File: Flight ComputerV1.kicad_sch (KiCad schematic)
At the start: 28 parts, among them J101 ICSP, J102 Screw_Terminal_01x02, J103 Conn_01x08, J104 Conn_01x07, J105 Micro_SD_Card, J106 Conn_02x10_Top_Bottom, SW101 1-1825910-8, U101 ATmega328PB-A, U102 LMT84DCK

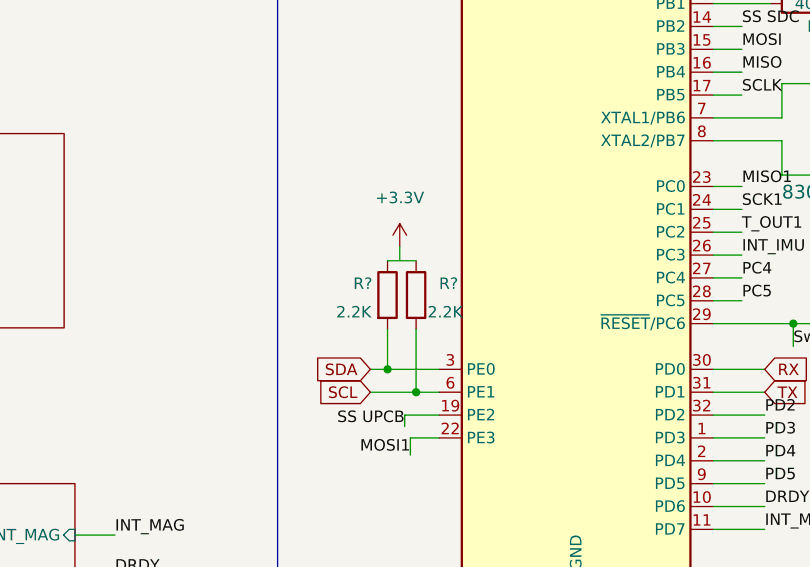
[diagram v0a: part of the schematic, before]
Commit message: Updated all trace widths and pull-up res.
I'm having a problem when I try to update the pcb with the pull-up resistors. Can you guys try updating the pcb, and let me know if you run into any errors?
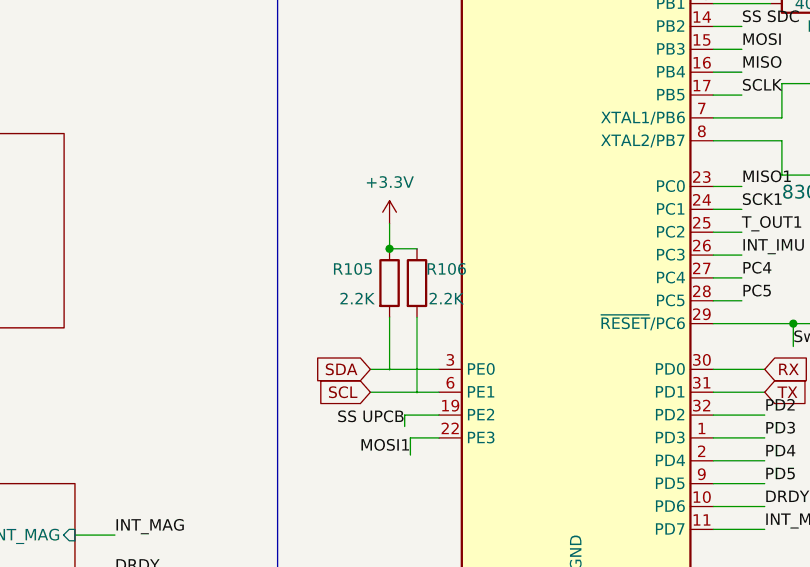
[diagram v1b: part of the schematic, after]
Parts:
- removed R? (x2): 2.2K, Resistor_SMD:R_0603_1608Metric_Pad0.98x0.95mm_HandSolder, symbol Device:R
- added R105, R106: 2.2K, Resistor_SMD:R_0603_1608Metric_Pad0.98x0.95mm_HandSolder, symbol Device:R
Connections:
- net +3V3: now also R105.1, R106.1

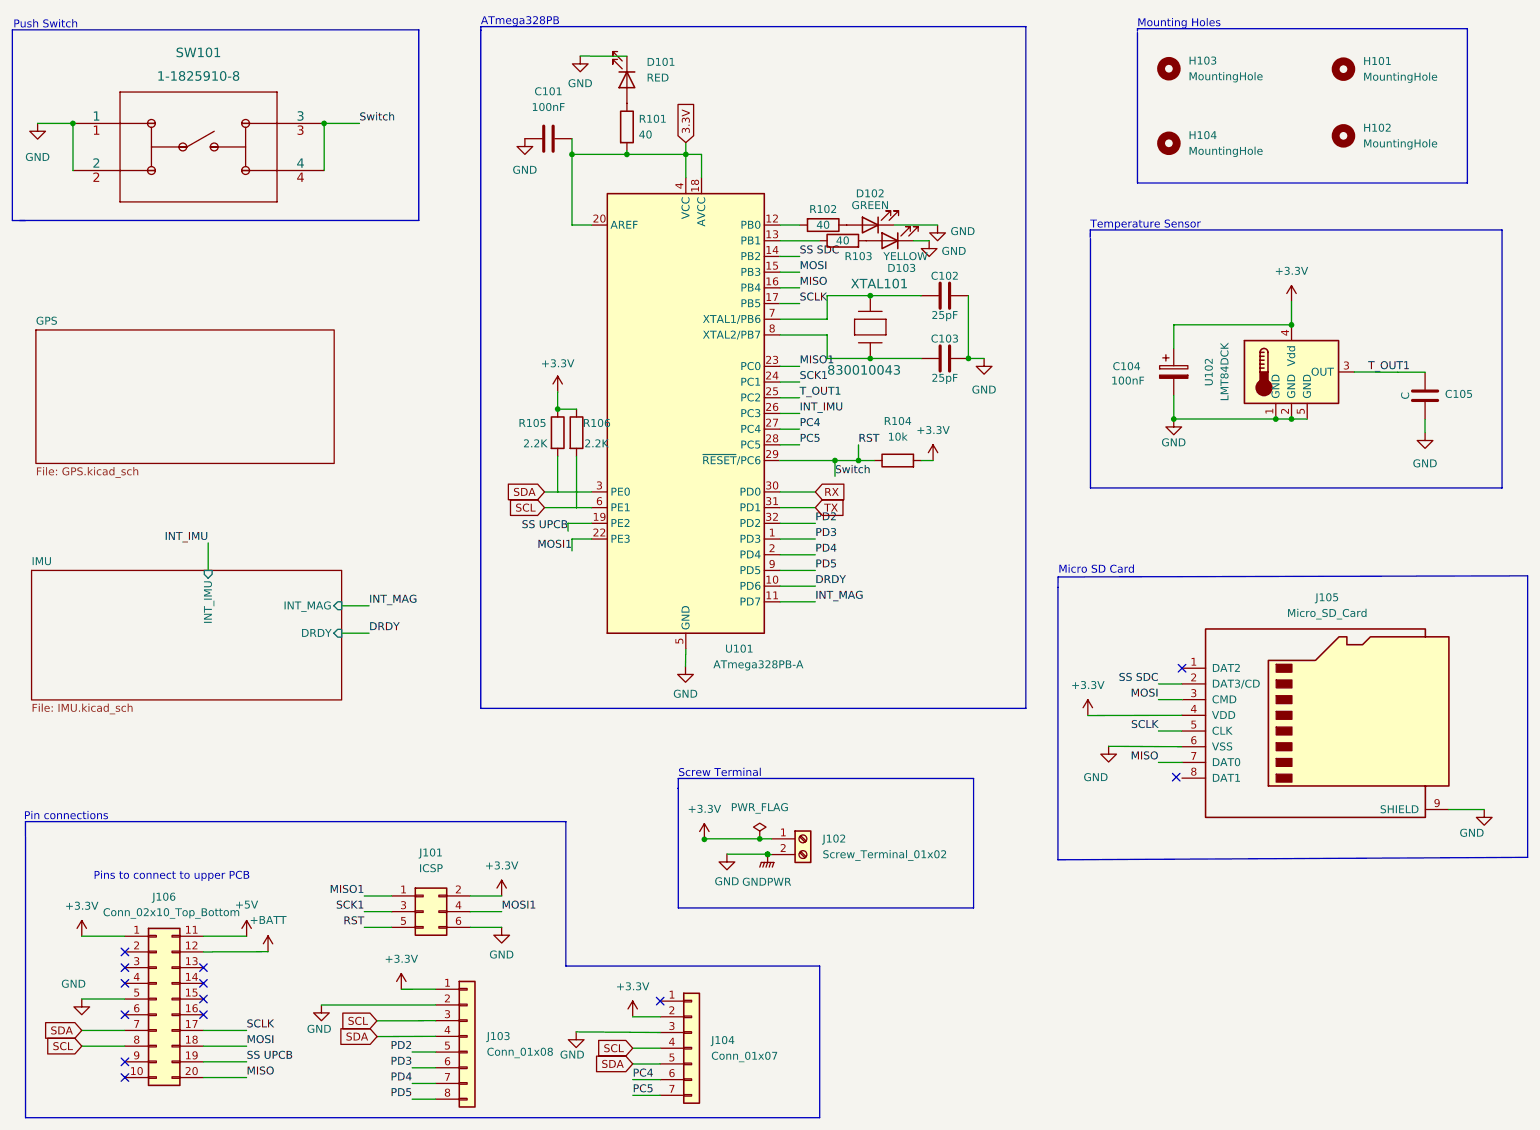
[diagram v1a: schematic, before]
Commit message: Updated pull-up resistors
Added pull-up resistors and testing github.
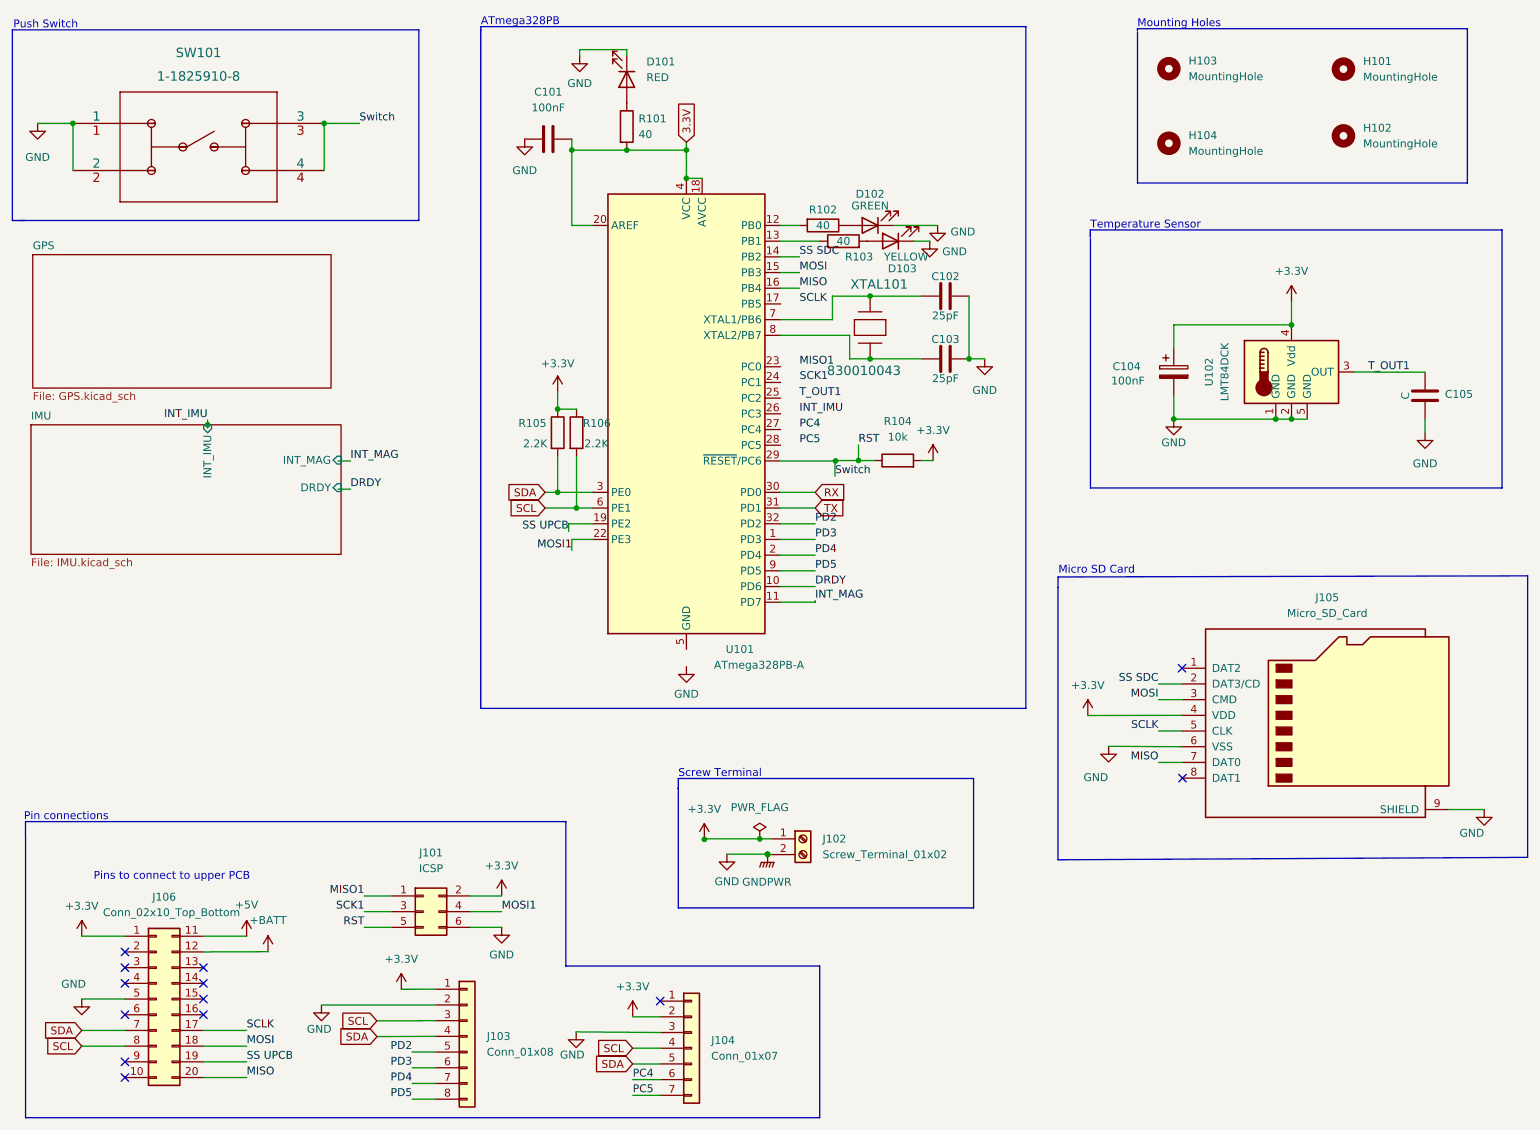
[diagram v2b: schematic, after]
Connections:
- net GND: no longer D102.1 (K), U101.21 (GND), U101.5 (GND)
- net INT_IMU: no longer U101.26 (PC3)
- net MISO1: no longer U101.23 (PC0)
- net PC4: no longer U101.27 (PC4)
- net PC5: no longer U101.28 (PC5)
- net RST: no longer U101.29 (~{RESET}/PC6)
- net SCK1: no longer U101.24 (PC1)
- net SCL: now also R106.2
- net SCLK: no longer U101.17 (PB5)
- net SDA: now also R105.2
- net T_OUT1: no longer U101.25 (PC2)
- new net: U101.21 (GND), U101.5 (GND)

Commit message: 10/18 changes
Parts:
- added TP1: MOSI, TestPoint:TestPoint_Pad_1.5x1.5mm, symbol Connector:TestPoint
- added TP10: TX, TestPoint:TestPoint_Pad_1.5x1.5mm, symbol Connector:TestPoint
- added TP11: GND, TestPoint:TestPoint_Pad_1.5x1.5mm, symbol Connector:TestPoint
- added TP12: 3.3V, TestPoint:TestPoint_Pad_1.5x1.5mm, symbol Connector:TestPoint
- added TP2: MISO, TestPoint:TestPoint_Pad_1.5x1.5mm, symbol Connector:TestPoint
- added TP3: SCLK, TestPoint:TestPoint_Pad_1.5x1.5mm, symbol Connector:TestPoint
- added TP4: SCK1, TestPoint:TestPoint_Pad_1.5x1.5mm, symbol Connector:TestPoint
- added TP5: MISO1, TestPoint:TestPoint_Pad_1.5x1.5mm, symbol Connector:TestPoint
- added TP6: MOSI1, TestPoint:TestPoint_Pad_1.5x1.5mm, symbol Connector:TestPoint
- added TP7: SDA, TestPoint:TestPoint_Pad_1.5x1.5mm, symbol Connector:TestPoint
- added TP8: SCL, TestPoint:TestPoint_Pad_1.5x1.5mm, symbol Connector:TestPoint
- added TP9: RX, TestPoint:TestPoint_Pad_1.5x1.5mm, symbol Connector:TestPoint
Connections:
- net 3.3V is gone; now on net +3V3: C101.2, R101.2, U101.18 (AVCC), U101.20 (AREF), U101.4 (VCC)
- net +3V3: now also TP12.1
- net GND: now also U101.21 (GND), U101.5 (GND), TP11.1
- net MISO: now also TP2.1
- net MISO1: now also TP5.1
- net MOSI: now also TP1.1
- net MOSI1: now also TP6.1
- net RX: now also TP9.1
- net SCK1: now also TP4.1
- net SCL: now also TP8.1
- net SCLK: now also U101.17 (PB5), TP3.1
- net SDA: now also TP7.1
- net TX: now also TP10.1
